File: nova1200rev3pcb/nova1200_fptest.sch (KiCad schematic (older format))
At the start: 174 parts, among them J1 Conn_02x26_Odd_Even, J2 Conn_02x05_Top_Bottom, J3 Conn_02x05_Top_Bottom, J4 Conn_02x01, SW1 SW_SPST, SW10 SW_SPST, SW11 SW_SPST, SW12 SW_SPST, SW13 SW_SPST, SW14 SW_SPST, SW15 SW_SPST, SW16 SW_SPST, SW17 SW_SPDT_MSM, SW18 SW_SPDT_MSM, SW19 SW_SPDT_MSM, SW2 SW_SPST, SW20 SW_SPDT_MSM, SW21 SW_SPDT_MSM, SW22 SW_SPDT_MSM, SW23 SW_SPDT_MSM, SW24 SW_SPDT_MSM, SW25 SW_SPDT_MSM, SW26 SW_SPDT_MSM, SW3 SW_SPST, SW4 SW_SPST, SW5 SW_SPST, SW6 SW_SPST, SW7 SW_SPST, SW8 SW_SPST, SW9 SW_SPST, U1 74LS257, U10 74LS173, U11 74LS173, U12 74LS173, U13 74LS173, U14 74LS173, U15 74LS257, U16 74LS42, U17 74LS42, U18 74LS02, U19 74LS06, U2 74LS257, U20 74LS06, U21 74LS06, U22 74LS173, U3 74LS257, U4 74LS257, U5 74LS173, U6 74LS173, U7 74LS173, U8 74LS173, U9 74LS173

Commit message: Removed bak files
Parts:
- R1, R10, R11, R12, R13, R14, R15, R16, R17, R18, R19, R2, R20, R21, R22, R23, R24, R25, R26, R27, R28, R29, R3, R30, R31, R32, R33, R34, R35, R36, R37, R38, R39, R4, R40, R41, R43, R45, R46, R47, R48, R49, R5, R50, R51, R52, R53, R54, R55, R57, R59, R6, R60, R61, R62, R63, R64, R65, R67, R68, R7, R8, R9: footprint Resistor_THT:R_Axial_DIN0204_L3.6mm_D1.6mm_P5.08mm_Horizontal -> Resistor_THT:R_Axial_DIN0204_L3.6mm_D1.6mm_P7.62mm_Horizontal
- U1, U10, U11, U12, U13, U14, U15, U16, U17, U2, U22, U3, U4, U5, U6, U7, U8, U9: footprint Package_DIP:DIP-16_W10.16mm -> Package_DIP:DIP-16_W7.62mm
- U18, U19, U20, U21: footprint Package_DIP:DIP-14_W10.16mm -> Package_DIP:DIP-14_W7.62mm

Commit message: Fixes and documentation of issues in rev3 fron panel PCB
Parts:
- removed C16, C17: C_Small, Capacitor_THT:CP_Radial_D5.0mm_P2.50mm, symbol Device:C_Small
- removed J2, J3: Conn_02x05_Top_Bottom, Connector_PinHeader_2.54mm:PinHeader_2x05_P2.54mm_Horizontal, symbol Connector_Generic:Conn_02x05_Top_Bottom
- removed J4: Conn_02x01, Connector_PinHeader_2.54mm:PinHeader_1x02_P2.54mm_Vertical, symbol Connector_Generic:Conn_02x01
- removed R32, R55, R57, R59, R60, R61, R62, R63, R64: 1K, Resistor_THT:R_Axial_DIN0204_L3.6mm_D1.6mm_P7.62mm_Horizontal, symbol Device:R_Small
- removed R65, R67, R68: 1M, Resistor_THT:R_Axial_DIN0204_L3.6mm_D1.6mm_P7.62mm_Horizontal, symbol Device:R_Small
- removed U1, U15, U2, U3, U4: 74LS257, Package_DIP:DIP-16_W7.62mm, symbol 74xx:74LS257
- removed U17: 74LS42, Package_DIP:DIP-16_W7.62mm, symbol 74xx:74LS42
- removed U18: 74LS02, Package_DIP:DIP-14_W7.62mm, symbol 74xx:74LS02
- removed U19, U20, U21: 74LS06, Package_DIP:DIP-14_W7.62mm, symbol 74xx:74LS06
- removed U22, U7, U8: 74LS173, Package_DIP:DIP-16_W7.62mm, symbol 74xx:74LS173
- added C16, C17, C18, C19: CP1_Small, Capacitor_THT:CP_Radial_Tantal_D5.0mm_P5.00mm, symbol Device:CP1_Small
- added D38, D39, D40, D41, D42, D43, D44, D45, D46, D47: LED_ALT, LED_THT:LED_D5.0mm_Clear, symbol Device:LED_ALT
- added H1, H2: MountingHole_Pad, MountingHole:MountingHole_2.2mm_M2_Pad, symbol Mechanical:MountingHole_Pad
- added J10, J13, J14, J20: Conn_01x01_Male, Connector_PinHeader_2.54mm:PinHeader_1x01_P2.54mm_Vertical, symbol Connector:Conn_01x01_Male
- added J11, J12, J15, J16, J17: Conn_01x04_Female, Connector_PinSocket_2.54mm:PinSocket_1x04_P2.54mm_Vertical, symbol Connector:Conn_01x04_Female
- added J18, J19: Conn_01x04_Male, Connector_PinSocket_2.54mm:PinSocket_1x04_P2.54mm_Vertical, symbol Connector:Conn_01x04_Male
- added J2: Conn_02x05_Odd_Even, Connector_PinHeader_2.54mm:PinHeader_2x08_P2.54mm_Vertical, symbol Connector_Generic:Conn_02x08_Odd_Even
- added J24: Conn_01x06_Male, Connector_PinHeader_2.54mm:PinHeader_1x06_P2.54mm_Vertical, symbol Connector:Conn_01x06_Male
- added J3: Conn_02x09_Odd Even, Connector_PinHeader_2.54mm:PinHeader_2x09_P2.54mm_Vertical, symbol Connector_Generic:Conn_02x09_Odd_Even
- added J4: Conn_01x02_Male, Connector_PinHeader_2.54mm:PinHeader_1x02_P2.54mm_Vertical, symbol Connector:Conn_01x02_Male
- added J5: Conn_01x03_Female, Connector_PinSocket_2.54mm:PinSocket_1x03_P2.54mm_Vertical, symbol Connector:Conn_01x03_Female
- added J6: Conn_02x05_Odd_Even, Connector_PinHeader_2.54mm:PinHeader_2x05_P2.54mm_Vertical, symbol Connector_Generic:Conn_02x05_Odd_Even
- added J7, J8: Conn_01x04, Connector_PinHeader_2.54mm:PinHeader_1x04_P2.54mm_Vertical, symbol Connector_Generic:Conn_01x04
- added J9: Conn_01x05_Male, Connector_PinHeader_2.54mm:PinHeader_1x05_P2.54mm_Vertical, symbol Connector:Conn_01x05_Male
- added PAD2, PAD4, PAD6: MountingHole_Pad, MountingHole:MountingHole_3.2mm_M3_Pad, symbol Mechanical:MountingHole_Pad
- added R38, R42, R44: 1K, Resistor_THT:R_Axial_DIN0204_L3.6mm_D1.6mm_P7.62mm_Horizontal, symbol Device:R_Small
- added R55, R56, R62, R63: 1K, Resistor_THT:R_Axial_DIN0204_L3.6mm_D1.6mm_P7.62mm_Horizontal, symbol Device:R
- added R57, R58, R59, R60, R61: 100K, Resistor_THT:R_Axial_DIN0204_L3.6mm_D1.6mm_P7.62mm_Horizontal, symbol Device:R
- added U1, U15, U2, U3, U4: MCP23017_SP, Package_DIP:DIP-28_W7.62mm, symbol Interface_Expansion:MCP23017_SP
- added U17, U19, U7, U8: 24LC1025, Package_DIP:DIP-8_W7.62mm, symbol Memory_EEPROM:24LC1025
- added U18: 4051, Package_DIP:DIP-16_W7.62mm, symbol 4xxx:4051
- added U20: LM7808_TO220, Package_TO_SOT_THT:TO-220-3_Horizontal_TabDown, symbol Regulator_Linear:LM7808_TO220
- added U21: 25LCxxx, Package_DIP:DIP-8_W7.62mm, symbol Memory_EEPROM:25LCxxx
- added U22: Teensy3.2, Teensy:Teensy30_31_32_LC, symbol nova1200_fptest-rescue:Teensy3.2-teensy
- added U23, U25: SFH617A-1, Package_DIP:DIP-4_W7.62mm, symbol Isolator:SFH617A-1
- added U24: 7402, Package_DIP:DIP-14_W7.62mm, symbol 74xx:7402
- R51: value 1M -> 1K
- renumbered H1 to FPIMAGE1, PAD5 to PAD3, PAD6 to PAD5, R38 to R32
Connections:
- net CONTDAT is gone; now on net CONTDATA: U10.1 (Oe1), U10.2 (Oe2), U5.1 (Oe1), U5.2 (Oe2), U6.1 (Oe1), U6.2 (Oe2), U9.1 (Oe1), U9.2 (Oe2)
- net KEYL is gone; now on net D0: A1.19 (A0)
- net KEYM is gone; now on net D1: A1.20 (A1)
- net LCD4 is gone; now on net D2: A1.21 (A2)
- net LCD5 is gone; now on net D3: A1.22 (A3)
- net SEL10 is gone; now on net SEL6: U13.7 (Cp)
- net SEL11 is gone; now on net SEL7: U14.7 (Cp)
- net SEL14 is gone; now on net SEL4: U11.7 (Cp)
- net SEL15 is gone; now on net SEL5: U12.7 (Cp)
- net SEL8 is gone; now on net SEL2: U9.7 (Cp)
- net SEL9 is gone; now on net SEL3: U10.7 (Cp)
- net SELR2 is gone; now on net A1: A1.12 (D9)
- net A0: now also A1.11 (D8), J6.3 (Pin_3), U22.8 (6_PWM); no longer A1.9 (D6)
- net A1: now also U22.9 (7_RX3_DOUT); no longer A1.10 (D7)
- net A2: now also U22.10 (8_TX3_DIN)
- net CARRY: now also U4.6 (GPB5)
- net D0: now also J6.5 (Pin_5), U22.25 (18_A4_SDA0_Touch); no longer A1.5 (D2)
- net D1: now also J6.6 (Pin_6), U22.26 (19_A5_SCL0_Touch); no longer A1.6 (D3)
- net D2: now also J6.7 (Pin_7), U22.27 (20_A6_CS_PWM); no longer A1.7 (D4)
- net D3: now also J5.3 (Pin_3), J6.8 (Pin_8), U22.28 (21_A7_RX1_CS_PWM); no longer A1.8 (D5)
- net DEFER: now also U4.4 (GPB3)
- net ENLCD1: now also A1.9 (D6), J6.4 (Pin_4), U22.6 (4_RX_PWM); no longer A1.15 (D12)
- net ENLCD2: now also A1.10 (D7), J6.10 (Pin_10), U22.7 (5_TX1_PWM); no longer A1.16 (D13)
- net EXEC: now also U4.5 (GPB4)
- net FETCH: now also U4.3 (GPB2)
- net GND: now also SW1.1 (A), SW10.1 (A), SW11.1 (A), SW12.1 (A), SW13.1 (A), SW14.1 (A), SW15.1 (A), SW16.1 (A), SW2.1 (A), SW3.1 (A), SW4.1 (A), SW5.1 (A), SW6.1 (A), SW7.1 (A), SW8.1 (A), SW9.1 (A), C16.2, C17.2, C18.2, C19.2, H1.1, H2.1, J11.1 (Pin_1), J12.1 (Pin_1), J15.1 (Pin_1), J16.1 (Pin_1), J17.1 (Pin_1), J18.1 (Pin_1), J19.1 (Pin_1), J2.1 (Pin_1), J20.1 (Pin_1), J24.1 (Pin_1), J3.1 (Pin_1), J5.1 (Pin_1), J6.1 (Pin_1), J7.1 (Pin_1), J9.1 (Pin_1), PAD2.1, PAD4.1, PAD6.1, R62.1, U1.10 (VSS), U1.17 (A2), U15.10 (VSS), U15.16 (A1), U15.17 (A2), U17.2 (A1), U17.4 (GND), U17.7 (WP), U18.6 (Inh), U18.7 (VEE), U18.8 (VSS), U19.4 (GND), U19.7 (WP), U2.10 (VSS), U2.15 (A0), U2.17 (A2), U20.2 (GND), U21.4 (GND), U22.1 (GND), U24.7 (GND), U25.2, U3.10 (VSS), U3.15 (A0), U3.16 (A1), U3.17 (A2), U4.10 (VSS), U4.15 (A0), U4.16 (A1), U7.1 (A0), U7.2 (A1), U7.4 (GND), U7.7 (WP), U8.1 (A0), U8.4 (GND), U8.7 (WP); no longer R50.1, R51.1
- net ION: now also U4.2 (GPB1)
- net NA1: now also U1.27 (GPA6)
- net NA10: now also U2.26 (GPA5)
- net NA11: now also U2.25 (GPA4)
- net NA12: now also U2.24 (GPA3)
- net NA13: now also U2.23 (GPA2)
- net NA14: now also U2.22 (GPA1)
- net NA15: now also U2.21 (GPA0)
- net NA2: now also U1.26 (GPA5)
- net NA3: now also U1.25 (GPA4)
- net NA4: now also U1.24 (GPA3)
- net NA5: now also U1.23 (GPA2)
- net NA6: now also U1.22 (GPA1)
- net NA7: now also U1.21 (GPA0)
- net NA8: now also U2.28 (GPA7)
- net NA9: now also U2.27 (GPA6)
- net ND0: now also U1.8 (GPB7); no longer SW16.1 (A)
- net ND1: now also U1.7 (GPB6); no longer SW15.1 (A)
- net ND10: now also U2.6 (GPB5); no longer SW6.1 (A)
- net ND11: now also U2.5 (GPB4); no longer SW5.1 (A)
- net ND12: now also U2.4 (GPB3); no longer SW4.1 (A)
- net ND13: now also U2.3 (GPB2); no longer SW3.1 (A)
- net ND14: now also U2.2 (GPB1); no longer SW2.1 (A)
- net ND15: now also U2.1 (GPB0); no longer SW1.1 (A)
- net ND2: now also U1.6 (GPB5); no longer SW14.1 (A)
- net ND3: now also U1.5 (GPB4); no longer SW13.1 (A)
- net ND4: now also U1.4 (GPB3); no longer SW12.1 (A)
- net ND5: now also U1.3 (GPB2); no longer SW11.1 (A)
- net ND6: now also U1.2 (GPB1); no longer SW10.1 (A)
- net ND7: now also U1.1 (GPB0); no longer SW9.1 (A)
- net ND8: now also U2.8 (GPB7); no longer SW8.1 (A)
- net ND9: now also U2.7 (GPB6); no longer SW7.1 (A)
- net RUN: now also U4.1 (GPB0)
- net SELR1: now also A1.8 (D5), U22.5 (3_TX_PWM); no longer A1.11 (D8)
- net VCC: now also C17.1, C18.1, C19.1, J11.2 (Pin_2), J12.2 (Pin_2), J15.2 (Pin_2), J16.2 (Pin_2), J17.2 (Pin_2), J18.2 (Pin_2), J19.2 (Pin_2), J4.1 (Pin_1), J5.2 (Pin_2), J6.2 (Pin_2), J7.4 (Pin_4), R55.1, R56.1, R57.1, R58.1, R59.1, R60.1, R61.1, U1.15 (A0), U1.16 (A1), U1.18 (~RESET~), U1.9 (VDD), U15.15 (A0), U15.18 (~RESET~), U15.9 (VDD), U17.1 (A0), U17.3 (A2), U17.8 (VCC), U18.16 (VDD), U19.1 (A0), U19.2 (A1), U19.3 (A2), U19.8 (VCC), U2.16 (A1), U2.18 (~RESET~), U2.9 (VDD), U24.14 (VCC), U3.18 (~RESET~), U3.9 (VDD), U4.17 (A2), U4.18 (~RESET~), U4.9 (VDD), U7.3 (A2), U7.8 (VCC), U8.2 (A1), U8.3 (A2), U8.8 (VCC); no longer C14.1, C8.1
- net VLAMP: now reaches J1.14 (Pin_14)
- net VLAMP: now also C8.1, U20.1 (VI)
- net SPIVCC: now reaches A1.18 (AREF)
- net SPIVCC: now also C16.1, J24.6 (Pin_6), J9.5 (Pin_5), U21.3 (~WP), U21.7 (~HOLD), U21.8 (VCC), U22.31 (3.3V_max100mA), U23.4
- net TA2: now reaches A1.26 (A7)
- net TA2: now also J6.9 (Pin_9), J9.2 (Pin_2), U22.23 (16_A2_SCL0_Touch)
- net at A1.27 (+5V): now also J10.1 (Pin_1)
- net at A1.30 (VIN): now also J14.1 (Pin_1)
- net at SW1.2 (B): now also U3.1 (GPB0)
- net at SW2.2 (B): now also U3.2 (GPB1)
- net at SW3.2 (B): now also U3.3 (GPB2)
- net at SW4.2 (B): now also U3.4 (GPB3)
- net at SW5.2 (B): now also U3.5 (GPB4)
- net at SW6.2 (B): now also U3.6 (GPB5)
- net at SW7.2 (B): now also U3.7 (GPB6)
- net at SW8.2 (B): now also U3.8 (GPB7)
- net at SW9.2 (B): now also U3.21 (GPA0)
- net at SW10.2 (B): now also U3.22 (GPA1)
- net at SW11.2 (B): now also U3.23 (GPA2)
- net at SW12.2 (B): now also U3.24 (GPA3)
- net at SW13.2 (B): now also U3.25 (GPA4)
- net at SW14.2 (B): now also U3.26 (GPA5)
- net at SW15.2 (B): now also U3.27 (GPA6)
- net at SW16.2 (B): now also U3.28 (GPA7)
- net at SW17.1: now also R48.2, SW18.1, SW19.1, SW20.1, SW21.1, J3.2 (Pin_2); no longer R39.2
- net at SW17.3: now also R49.2, SW18.3, SW19.3, SW20.3, SW21.3, J3.18 (Pin_18); no longer R40.2
- net at SW23.1: now also R50.2, SW22.1, SW24.1, SW25.1, SW26.1, J3.16 (Pin_16); no longer R53.1
- net at SW23.3: now also R51.2, SW22.3, SW24.3, SW25.3, SW26.3, J3.4 (Pin_4); no longer R54.1
- net A0' renamed ENOLED0
- net ENOLED0: now also U18.11 (A), U22.11 (9_RX2_CS_PWM)
- net AREF: no longer names the net of R49.1
- net AREF: now also U15.22 (GPA1)
- net ENSWREG: no longer names the net of U13.6 (Q3)
- net KEYP renamed TA3
- net TA3: now also J9.3 (Pin_3), U22.24 (17_A3_SDA0_Touch)
- net LCD6 renamed SDA
- net SDA: now also J18.4 (Pin_4), J19.3 (Pin_3), R55.2, U1.13 (SDA), U15.13 (SDA), U17.5 (SDA), U18.3 (X), U19.5 (SDA), U2.13 (SDA), U22.29 (22_A8_Touch_PWM), U3.13 (SDA), U4.13 (SDA), U7.5 (SDA), U8.5 (SDA)
- net LCD7 renamed SCK
- net SCK: now also J11.3 (Pin_3), J12.3 (Pin_3), J15.3 (Pin_3), J16.3 (Pin_3), J17.3 (Pin_3), J18.3 (Pin_3), J19.4 (Pin_4), R56.2, U1.12 (SCK), U15.12 (SCK), U17.6 (SCL), U19.6 (SCL), U2.12 (SCK), U22.30 (23_A9_Touch_PWM), U3.12 (SCK), U4.12 (SCK), U7.6 (SCL), U8.6 (SCL)
- new net: D38.2 (A), D43.2 (A), J3.5 (Pin_5), SW17.2, SW22.2, U15.5 (GPB4)
- new net: D39.2 (A), D44.2 (A), J3.9 (Pin_9), SW18.2, SW23.2, U15.4 (GPB3)
- new net: D40.2 (A), D45.2 (A), J3.15 (Pin_15), SW19.2, SW24.2, U15.3 (GPB2)
- new net: D41.2 (A), D46.2 (A), J3.13 (Pin_13), SW20.2, SW25.2, U15.2 (GPB1)
- new net: D42.2 (A), D47.2 (A), J3.14 (Pin_14), SW21.2, SW26.2, U15.1 (GPB0)
- new net: J3.10 (Pin_10), U15.28 (GPA7)
- new net: J3.11 (Pin_11), R54.2
- new net: J3.12 (Pin_12), U15.6 (GPB5)
- new net: J3.3 (Pin_3), R52.2
- new net: J3.6 (Pin_6), R43.1, R44.1, R45.1, R46.1, R47.1, U15.7 (GPB6)
- new net: J3.7 (Pin_7), R53.2
- new net: J3.8 (Pin_8), R38.1, R39.1, R40.1, R41.1, R42.1, U15.8 (GPB7)
- new net: R48.1, U15.21 (GPA0)
- new net: R50.1, U15.23 (GPA2)
- new net: R51.1, U15.24 (GPA3)
- new net: R52.1, U15.25 (GPA4)
- new net: R53.1, U15.26 (GPA5)
- new net: R54.1, U15.27 (GPA6)
- new net: D43.1 (K), R43.2
- new net: D44.1 (K), R44.2
- new net: D45.1 (K), R45.2
- new net: D46.1 (K), R46.2
- new net: D47.1 (K), R47.2
- new net: D38.1 (K), R38.2
- new net: D39.1 (K), R39.2
- new net: D40.1 (K), R40.2
- new net: D41.1 (K), R41.2
- new net: D42.1 (K), R42.2
- new net: J11.4 (Pin_4), R57.2, U18.13 (X0)
- new net: J12.4 (Pin_4), R58.2, U18.14 (X1)
- new net: J15.4 (Pin_4), R59.2, U18.15 (X2)
- new net: J16.4 (Pin_4), R60.2, U18.12 (X3)
- new net: J17.4 (Pin_4), R61.2, U18.1 (X4)
- new net: J2.13 (Pin_13), U24.2, U4.20 (INTA)
- new net: J2.4 (Pin_4), U4.21 (GPA0)
- new net: J2.6 (Pin_6), U4.22 (GPA1)
- new net: J2.8 (Pin_8), U4.23 (GPA2)
- new net: J2.10 (Pin_10), U4.24 (GPA3)
- new net: J2.12 (Pin_12), U4.25 (GPA4)
- new net: J2.14 (Pin_14), U4.26 (GPA5)
- new net: J2.16 (Pin_16), U4.27 (GPA6)
- new net: J2.15 (Pin_15), U4.28 (GPA7)
- new net: J2.11 (Pin_11), U24.13, U24.8
- new net: J2.2 (Pin_2), U24.3, U24.4
- new net: J2.3 (Pin_3), U24.5
- new net: J2.5 (Pin_5), U24.10, U24.11
- new net: J2.7 (Pin_7), U24.12
- new net: J2.9 (Pin_9), U24.9
- new net: C14.1, J13.1 (Pin_1), U20.3 (VO)
- new net: J4.2 (Pin_2), U22.33 (Vin)
- new net: U24.1, U24.6
- new net: J8.1 (Pin_1), U23.1
- new net: J8.2 (Pin_2), U23.2
- new net: R63.2, U25.1
- new net: J8.4 (Pin_4), U25.3
- new net: J8.3 (Pin_3), U25.4
- new net A14: J9.4 (Pin_4), U22.19 (A14/DAC)
- new net CS: J24.5 (Pin_5), U21.1 (~CS), U22.21 (14_A0_SCK)
- new net ENOLED1: A1.15 (D12), U18.10 (B), U22.12 (10_TX2_CS_PWM)
- new net ENOLED2: A1.16 (D13), U18.9 (C), U22.22 (15_A1_CS_Touch)
- new net KEYINT: U15.20 (INTA), U4.7 (GPB6)
- new net LIGHTINT: A1.5 (D2), U22.4 (2), U4.19 (INTB)
- new net MISO: J24.2 (Pin_2), U21.2 (MISO), U22.14 (12_DIN)
- new net MOSI: J24.3 (Pin_3), U21.5 (MOSI), U22.13 (11_DOUT)
- new net SERIALIN: A1.6 (D3), J7.3 (Pin_3), R62.2, U22.2 (0_RX1_Touch), U23.3
- new net SERIALOUT: A1.7 (D4), J7.2 (Pin_2), R63.1, U22.3 (1_TX1_Touch)
- new net SSCK: J24.4 (Pin_4), U21.6 (SCK), U22.20 (13_LED_SCK)
- new net SWINT: U3.20 (INTA), U4.8 (GPB7)
- no-connect marks 31 -> 55
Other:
- note added: "3.3V"
- note added: "433.92 sender"
- note added: "74ls173 Register list:\n0 = write lsb data 12-15\n1 = write lsb data 8-11\n2 = write msb data 4-7\n3 = write msb data 0-3\n4 = write inst 12-15\n5 = write inst 8-11\n6 = write control L\n7 = write control H\n\n"
- note added: "A1"
- note added: "A2"
- note added: "A3"
- note added: "A4"
- note added: "A5"
- note added: "A6"
- note added: "A7"
- note added: "A8"
- note added: "A9"
- note added: "AGND"
- note added: "D0"
- note added: "D1"
- note added: "D10"
- note added: "D2"
- note added: "D3"
- note added: "D4"
- note added: "D5"
- note added: "D6"
- note added: "D7"
- note added: "D8"
- note added: "D9"
- note added: "Disconnect for teensy4"
- note added: "INTR (low)"
- note added: "IOCLR (high)"
- note added: "Keypad (odd pins) and/or switch bank"
- note added: "LCD"
- note added: "LSB"
- note added: "MSB"
- note added: "Move to 3.3V for Teensy4"
- note added: "NC"
- note added: "OLED Displays 1-5"
- note added: "Register list I2C:\n20-12 switches high\n20-13 switches low\n21-12 key sense\n21-13 key select + leds\n22-12 addr low\n23-12 add high\n22-13 data low\n23-13 data high\n24-12 interupts (unused)\n24-13 lights\n3C = OLED\n50 = EEPROM0\n"
- note added: "Register list I2C\n0 = read data switches\n1 = read control switches\n2 = read low data address\n3 = read high data address\n4 = read lights & interrupt\n\n"
- note added: "SPI"
- note added: "VIN"
- note added: "analog"
- note added: "current\nloop"
- note added: "kpad"
- note added: "serial"
- note added: "teensy"
- note removed: "INST L\n(optional)"
- note removed: "Keypad"
- note removed: "Read\nDATA/ADDR LSB 8-15"
- note removed: "Read\nDATA/ADDR MSB 0-7"
- note removed: "Read\nSTATUS"
- note removed: "Register list LSB:\n0 = write lsb data 12-15\n1 = write lsb data 8-11\n2 = write lsb inst 12-15 (optional)\n3 = write lsb inst 8-11 (optional)\n4 = read data lsb 12-15\n5 = read data lsb 8-11\n6 = read status 0-3\n7 = spare\n20 = read addr lsb 12-15\n21 = read addr lsb 8-11\n22= read status 4\n"
- note removed: "Register list MSB:\n8 = write msb data 4-7\n9 = write msb data 0-3\n10 = write control 5-7\n11 = write control 0-3\n12 = read data msb 4-7\n13 = read data msb 0-3\n14 = write msb inst 4-7\n15 = write msb inst 0-3\n28 = read addr msb 4-7\n29 = read addr msb 0-3\n"
- note removed: "Remove jumper when Arduino connected to PC"
- note removed: "spare inputs"
- note removed: "spare outputs"
- note removed: "vlamp"
- moved on the sheet: A1, C1, C10, C11, C12, C13, C15, C3, C5, C7, C9, FPIMAGE1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

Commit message: Updated todo list in schematic (mainly for 3.3 volt operation)
3v3 vs 5v jumper at DWP\nLevel shifter for I2C connection, lightint\nCheck SPI connector conforms to IL9341 display\nFix few bugs under dotted boxes\nCan it drive original front panel?\nRemove arduino socket?
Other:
- note added: "Todo: 3v3 vs 5v jumper at DWP\nLevel shifter for I2C connection, lightint\nCheck SPI connector conforms to IL9341 display\nFix few bugs under dotted boxes\nCan it drive original front panel?\nRemove arduino socket?"
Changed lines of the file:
@@
 Text Notes 10650 6100 0    50   ~ 0
 Move to 3.3V for Teensy4
+Text Notes 2400 10850 0    50   ~ 0
+Todo: 3v3 vs 5v jumper at DWP\nLevel shifter for I2C connection, lightint\nCheck SPI connector conforms to IL9341 display\nFix few bugs under dotted boxes\nCan it drive original front panel?\nRemove arduino socket?
 $EndSCHEMATC

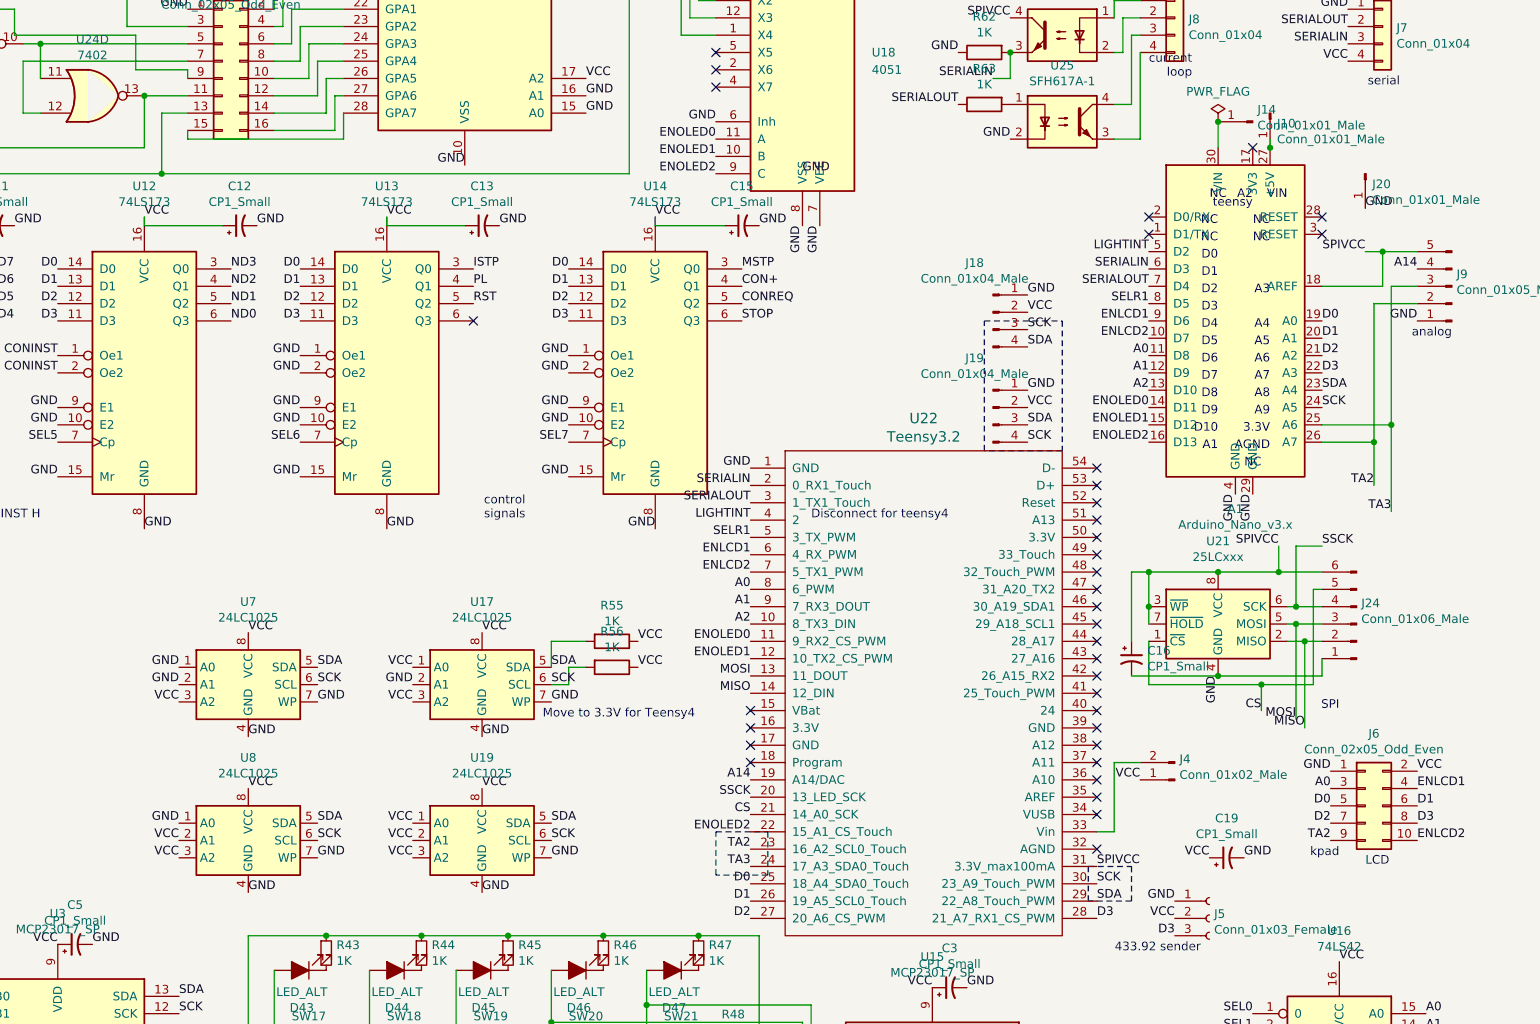
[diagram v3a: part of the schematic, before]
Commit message: Modified rev3 PCB for Teensy4.1 and Maker Nano RP2040 compatibility
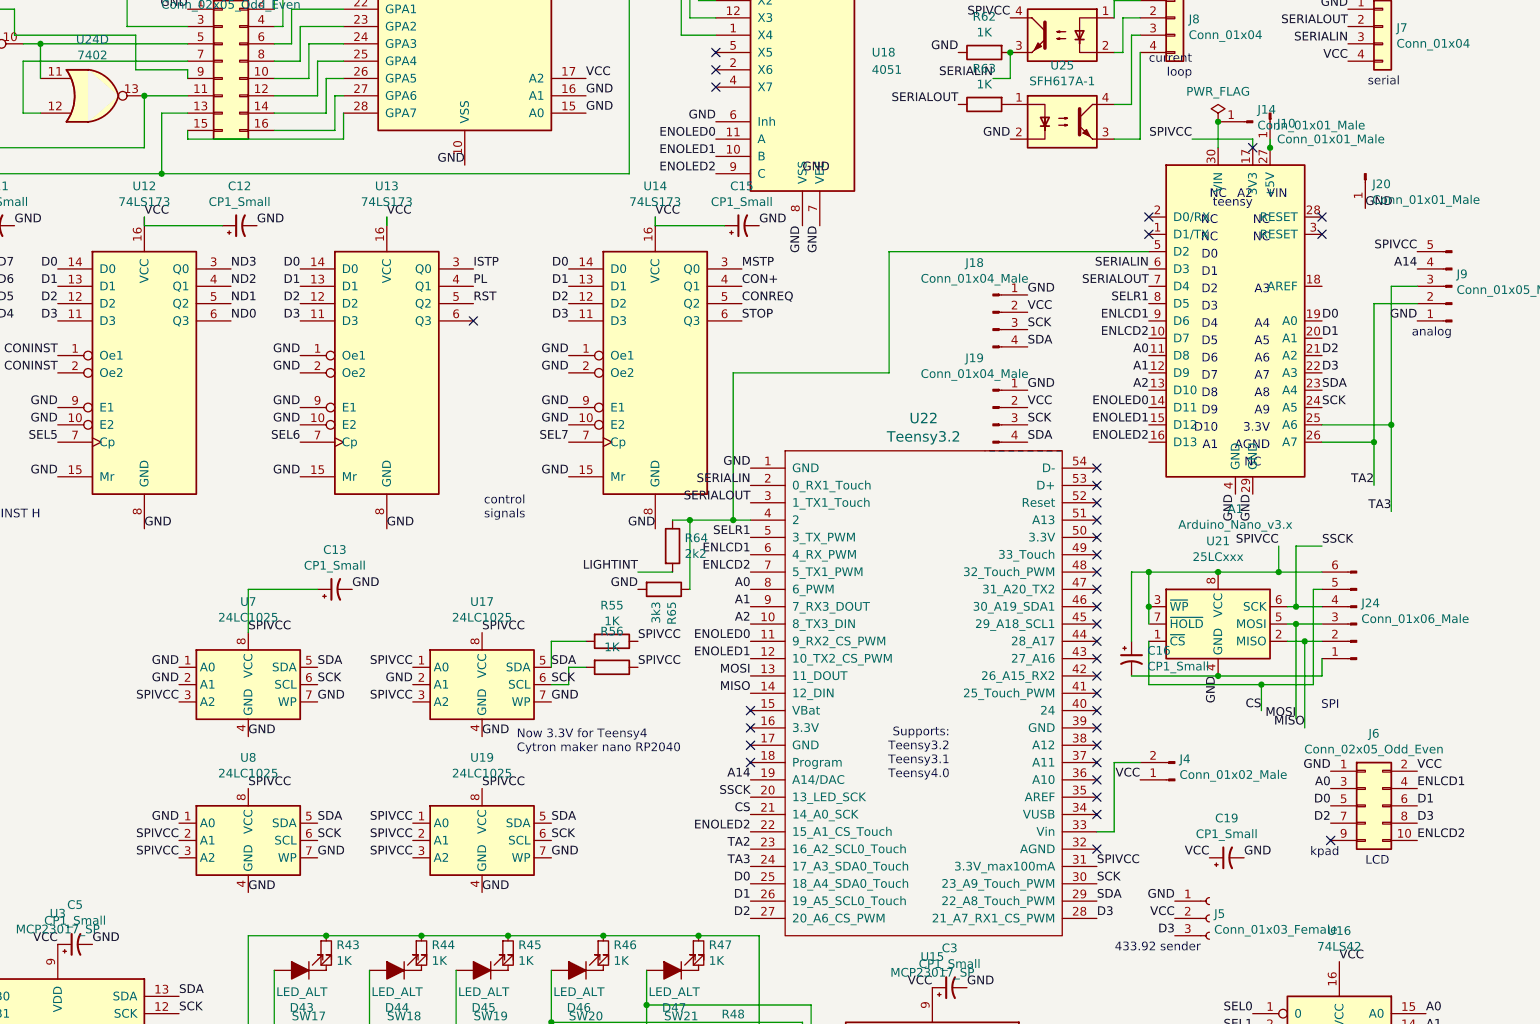
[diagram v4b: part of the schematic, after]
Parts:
- added R64: 2k2, Resistor_THT:R_Axial_DIN0204_L3.6mm_D1.6mm_P7.62mm_Horizontal, symbol Device:R
- added R65: 3k3, Resistor_THT:R_Axial_DIN0204_L3.6mm_D1.6mm_P7.62mm_Horizontal, symbol Device:R
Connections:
- net GND: now also R65.2
- net LIGHTINT: now also R64.2; no longer A1.5 (D2), U22.4 (2)
- net SCK: now also J19.3 (Pin_3); no longer J19.4 (Pin_4)
- net SDA: now also J19.4 (Pin_4); no longer J19.3 (Pin_3)
- net SPIVCC: now also A1.17 (3V3), C13.1, R55.1, R56.1, U17.1 (A0), U17.3 (A2), U17.8 (VCC), U19.1 (A0), U19.2 (A1), U19.3 (A2), U19.8 (VCC), U7.3 (A2), U7.8 (VCC), U8.2 (A1), U8.3 (A2), U8.8 (VCC); no longer A1.18 (AREF)
- net TA2: no longer J6.9 (Pin_9)
- net VCC: no longer C13.1, R55.1, R56.1, U17.1 (A0), U17.3 (A2), U17.8 (VCC), U19.1 (A0), U19.2 (A1), U19.3 (A2), U19.8 (VCC), U7.3 (A2), U7.8 (VCC), U8.2 (A1), U8.3 (A2), U8.8 (VCC)
- new net: A1.5 (D2), R64.1, R65.1, U22.4 (2)
- no-connect marks 55 -> 56
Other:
- note added: "Now 3.3V for Teensy4\nCytron maker nano RP2040"
- note added: "Supports:\nTeensy3.2\nTeensy3.1\nTeensy4.0"
- note removed: "Disconnect for teensy4"
- note removed: "Move to 3.3V for Teensy4"
- moved on the sheet: C13
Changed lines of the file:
@@
 Sheet 1 1
 Title "Computer controlled front panel for Nova 1200 computer"
-Date "2019-05-12"
-Rev "2a"
+Date "2024-01-23"
+Rev "2b"
 Comp "Marcel van Herk"
-Comment1 "Using multicomp switches; swapped lightint and serial"
+Comment1 "Using multicomp switches; swapped lightint and serial; Teensy4 compatible; fix J19"
 Comment2 "Fix: C19 in wrong place for teensy Vin, now VCC; r42 misconnected"
 Comment3 "Error: switch holes too small, optional 7808 touches tracks, swap J3 11, 15"
@@
 Text Label 11900 3250 0    50   ~ 0
 GND
-Text Label 10400 3250 0    50   ~ 0
+Text Label 9550 5350 0    50   ~ 0
 GND
 Text Label 9000 3250 0    50   ~ 0
@@
 	8350 3250 8350 3200
 Wire Wire Line
-	10200 3250 9750 3250
-Wire Wire Line
 	9750 3250 9750 3200
 Wire Wire Line
@@
 L Device:CP1_Small C13
 U 1 1 5C3D947E
-P 10300 3250
-F 0 "C13" V 10528 3250 50  0000 C CNN
-F 1 "CP1_Small" V 10437 3250 50  0000 C CNN
-F 2 "Capacitor_THT:CP_Radial_Tantal_D5.0mm_P5.00mm" H 10300 3250 50  0001 C CNN
-F 3 "~" H 10300 3250 50  0001 C CNN
-	1    10300 3250
+P 9450 5350
+F 0 "C13" V 9678 5350 50  0000 C CNN
+F 1 "CP1_Small" V 9587 5350 50  0000 C CNN
+F 2 "Capacitor_THT:CP_Radial_Tantal_D5.0mm_P5.00mm" H 9450 5350 50  0001 C CNN
+F 3 "~" H 9450 5350 50  0001 C CNN
+	1    9450 5350
 	0    -1   -1   0
 $EndComp
@@
 $EndComp
 Text Label 8950 5600 0    50   ~ 0
-VCC
+SPIVCC
 Text Label 8550 5800 2    50   ~ 0
 GND
@@
 GND
 Text Label 8550 6000 2    50   ~ 0
-VCC
+SPIVCC
 Text Label 9350 5800 0    50   ~ 0
 SDA
@@
 $EndComp
 Text Label 10300 5600 0    50   ~ 0
-VCC
+SPIVCC
 Text Label 9900 5800 2    50   ~ 0
-VCC
+SPIVCC
 Text Label 9900 5900 2    50   ~ 0
 GND
 Text Label 9900 6000 2    50   ~ 0
-VCC
+SPIVCC
 Text Label 10700 5800 0    50   ~ 0
 SDA
@@
 $EndComp
 Text Label 8950 6500 0    50   ~ 0
-VCC
+SPIVCC
 Text Label 8550 6700 2    50   ~ 0
 GND
 Text Label 8550 6800 2    50   ~ 0
-VCC
+SPIVCC
 Text Label 8550 6900 2    50   ~ 0
-VCC
+SPIVCC
 Text Label 9350 6700 0    50   ~ 0
 SDA
@@
 $EndComp
 Text Label 10300 6500 0    50   ~ 0
-VCC
+SPIVCC
 Text Label 9900 6700 2    50   ~ 0
-VCC
+SPIVCC
 Text Label 9900 6800 2    50   ~ 0
-VCC
+SPIVCC
 Text Label 9900 6900 2    50   ~ 0
-VCC
+SPIVCC
 Text Label 10700 6700 0    50   ~ 0
 SDA
@@
 Text Label 15300 2300 2    50   ~ 0
 VCC
-Text Label 14150 3400 2    50   ~ 0
-LIGHTINT
 $Comp
 L Interface_Expansion:MCP23017_SP U4
@@
 Text Label 13450 3950 0    50   ~ 0
 SDA
-Text Label 13450 4400 0    50   ~ 0
-SDA
 Text Label 13450 4500 0    50   ~ 0
+SDA
+Text Label 13450 4400 0    50   ~ 0
 SCK
 $Comp
@@
 $EndComp
 Text Label 11200 5650 0    50   ~ 0
-VCC
+SPIVCC
 Text Label 11200 5800 0    50   ~ 0
-VCC
+SPIVCC
 Wire Wire Line
 	10700 5800 10700 5650
@@
 Text Label 11850 4650 2    50   ~ 0
 GND
-Text Label 11850 4950 2    50   ~ 0
+Text Label 11200 5250 2    50   ~ 0
 LIGHTINT
 Text Label 11850 4750 2    50   ~ 0
@@
 Text Label 15450 4750 2    50   ~ 0
 TA2
-Wire Wire Line
-	15500 3400 15400 3400
-Text Label 15400 3400 2    50   ~ 0
+Text Label 15700 3400 2    50   ~ 0
 SPIVCC
 Wire Wire Line
-	15500 3400 15700 3400
-Connection ~ 15500 3400
-Wire Wire Line
-	15150 3600 15500 3600
-Wire Wire Line
-	15500 3400 15500 3600
-Wire Wire Line
 	15150 4400 15550 4400
 Wire Wire Line
@@
 Text Label 1700 9900 0    50   ~ 0
 GND
-Text Label 15200 6800 2    50   ~ 0
-TA2
 Text Label 14500 6900 2    50   ~ 0
 VCC
@@
 	10150 9500 10150 9150
 Wire Notes Line
-	13200 3800 13650 3800
-Wire Notes Line
 	13650 4550 13200 4550
-Wire Notes Line
-	13200 4550 13200 3800
-Wire Notes Line
-	13650 3800 13650 4550
-Wire Notes Line
-	11950 6750 11950 7000
-Wire Notes Line
-	11950 7000 11650 7000
-Wire Notes Line
-	11650 7000 11650 6750
-Wire Notes Line
-	11650 6750 11950 6750
-Wire Notes Line
-	14050 7150 13800 7150
-Wire Notes Line
-	13800 7150 13800 6950
-Wire Notes Line
-	13800 6950 14050 6950
-Wire Notes Line
-	14050 6950 14050 7150
 $Comp
 L Isolator:SFH617A-1 U23
@@
 Text Notes 13850 9850 0    50   ~ 0
 Register list I2C:\n20-12 switches high\n20-13 switches low\n21-12 key sense\n21-13 key select + leds\n22-12 addr low\n23-12 add high\n22-13 data low\n23-13 data high\n24-12 interupts (unused)\n24-13 lights\n3C = OLED\n50 = EEPROM0\n
-Text Notes 12200 4950 0    50   ~ 0
-Disconnect for teensy4
-Text Notes 10650 6100 0    50   ~ 0
-Move to 3.3V for Teensy4
+Text Notes 10500 6300 0    50   ~ 0
+Now 3.3V for Teensy4\nCytron maker nano RP2040
 Text Notes 2400 10850 0    50   ~ 0
 Todo: 3v3 vs 5v jumper at DWP\nLevel shifter for I2C connection, lightint\nCheck SPI connector conforms to IL9341 display\nFix few bugs under dotted boxes\nCan it drive original front panel?\nRemove arduino socket?
+$Comp
+L Device:R R64
+U 1 1 65B83E33
+P 11400 5100
+F 0 "R64" H 11470 5146 50  0000 L CNN
+F 1 "2k2" H 11470 5055 50  0000 L CNN
+F 2 "Resistor_THT:R_Axial_DIN0204_L3.6mm_D1.6mm_P7.62mm_Horizontal" V 11330 5100 50  0001 C CNN
+F 3 "~" H 11400 5100 50  0001 C CNN
+	1    11400 5100
+	1    0    0    -1
+$EndComp
+Wire Wire Line
+	11400 4950 11500 4950
+Wire Wire Line
+	11400 5250 11200 5250
+Wire Wire Line
+	11750 4950 11750 4100
+Wire Wire Line
+	11750 4100 12650 4100
+Wire Wire Line
+	12650 4100 12650 3400
+Wire Wire Line
+	12650 3400 14150 3400
+Connection ~ 11750 4950
+Wire Wire Line
+	11750 4950 11850 4950
+Wire Wire Line
+	11500 4950 11500 5350
+Connection ~ 11500 4950
+Wire Wire Line
+	11500 4950 11750 4950
+$Comp
+L Device:R R65
+U 1 1 65B770FF
+P 11350 5350
+F 0 "R65" H 11420 5396 50  0000 L CNN
+F 1 "3k3" H 11420 5305 50  0000 L CNN
+F 2 "Resistor_THT:R_Axial_DIN0204_L3.6mm_D1.6mm_P7.62mm_Horizontal" V 11280 5350 50  0001 C CNN
+F 3 "~" H 11350 5350 50  0001 C CNN
+	1    11350 5350
+	0    1    1    0
+$EndComp
+Text Label 11200 5350 2    50   ~ 0
+GND
+NoConn ~ 15200 6800
+Text Notes 13000 6450 2    50   ~ 0
+Supports:\nTeensy3.2\nTeensy3.1\nTeensy4.0
+Wire Wire Line
+	14750 2800 14750 2750
+Text Label 14400 2750 2    50   ~ 0
+SPIVCC
+Wire Wire Line
+	14750 2750 14400 2750
+Wire Wire Line
+	9350 5350 8950 5350
+Wire Wire Line
+	8950 5350 8950 5600
 $EndSCHEMATC

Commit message: Moved LCD displays to SPIVCC, use 74HCT4051, plot
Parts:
- U18: value 4051 -> 74HCT4051
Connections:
- net SPIVCC: now also C19.1, J11.2 (Pin_2), J12.2 (Pin_2), J15.2 (Pin_2), J16.2 (Pin_2), J17.2 (Pin_2), J18.2 (Pin_2), J19.2 (Pin_2), R57.1, R58.1, R59.1, R60.1, R61.1
- net VCC: no longer C19.1, J11.2 (Pin_2), J12.2 (Pin_2), J15.2 (Pin_2), J16.2 (Pin_2), J17.2 (Pin_2), J18.2 (Pin_2), J19.2 (Pin_2), R57.1, R58.1, R59.1, R60.1, R61.1
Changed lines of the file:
@@
 GND
 Text Label 11550 900  0    50   ~ 0
-VCC
+SPIVCC
 $Comp
 L Connector:Conn_01x04_Female J12
@@
 GND
 Text Label 12350 900  0    50   ~ 0
-VCC
+SPIVCC
 $Comp
 L Connector:Conn_01x04_Female J15
@@
 GND
 Text Label 13200 900  0    50   ~ 0
-VCC
+SPIVCC
 $Comp
 L Connector:Conn_01x04_Female J16
@@
 GND
 Text Label 14000 900  0    50   ~ 0
-VCC
+SPIVCC
 $Comp
 L Connector:Conn_01x04_Female J17
@@
 GND
 Text Label 14800 900  0    50   ~ 0
-VCC
+SPIVCC
 Wire Wire Line
 	11550 1100 11850 1100
@@
 GND
 Text Label 13450 3750 0    50   ~ 0
-VCC
+SPIVCC
 Text Label 13450 4300 0    50   ~ 0
-VCC
+SPIVCC
 Text Label 13450 3850 0    50   ~ 0
 SCK
@@
 P 12150 2350
 F 0 "U18" H 12550 2450 50  0000 L CNN
-F 1 "4051" H 12550 2350 50  0000 L CNN
+F 1 "74HCT4051" H 12550 2350 50  0000 L CNN
 F 2 "Package_DIP:DIP-16_W7.62mm" H 12150 2350 50  0001 C CNN
 F 3 "http://www.intersil.com/content/dam/Intersil/documents/cd40/cd4051bms-52bms-53bms.pdf" H 12150 2350 50  0001 C CNN
@@
 Connection ~ 12700 1200
 Text Label 12150 1300 0    50   ~ 0
-VCC
+SPIVCC
 Text Label 13000 1200 0    50   ~ 0
-VCC
+SPIVCC
 Text Label 13750 1300 0    50   ~ 0
-VCC
+SPIVCC
 Text Label 14550 1300 0    50   ~ 0
-VCC
+SPIVCC
 Text Label 15350 1300 0    50   ~ 0
-VCC
+SPIVCC
 Text Notes 14550 3450 2    50   ~ 0
 D0
@@
 GND
 Text Label 14500 6900 2    50   ~ 0
-VCC
+SPIVCC
 Wire Wire Line
 	15000 5450 15000 5100
